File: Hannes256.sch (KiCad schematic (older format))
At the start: 7 parts, among them J1 TED_SOCKET, J2 RAM_SELECTOR, J3 CONN_CS, U1 MOS_7360_TED

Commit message: Routing in progress
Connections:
- net MUX renamed mux
- net clkout renamed CLKOUT
- net ~RAS renamed ~ras

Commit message: ROuting done
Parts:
- added V0: CC_LOGO, Hannes256:cc_by_nc_sa, symbol void:Void
- V1: renamed from V0; value CC_LOGO -> LOGO; footprint Hannes256:cc_by_nc_sa -> Hannes256:logo
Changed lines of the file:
@@
 Sheet 1 3
 Title "Hannes256: C16/+4 256 kB RAM Expansion"
-Date "2023-02-21"
+Date "2023-02-27"
 Rev "3git"
 Comp "SukkoPera"
@@
 $EndComp
 $Comp
-L void:Void V0
+L void:Void V1
 U 1 1 63C4EC1B
 P 15540 9765
-F 0 "V0" H 15618 9811 50  0000 L CNN
-F 1 "CC_LOGO" H 15618 9720 50  0000 L CNN
-F 2 "Hannes256:cc_by_nc_sa" H 15540 9765 50  0001 C CNN
+F 0 "V1" H 15618 9811 50  0000 L CNN
+F 1 "LOGO" H 15618 9720 50  0000 L CNN
+F 2 "Hannes256:logo" H 15540 9765 50  0001 C CNN
 F 3 "" H 15540 9765 50  0001 C CNN
 	1    15540 9765
@@
 Wire Bus Line
 	10425 2375 10425 4285
+$Comp
+L void:Void V0
+U 1 1 64911216
+P 15540 9560
+F 0 "V0" H 15618 9606 50  0000 L CNN
+F 1 "CC_LOGO" H 15618 9515 50  0000 L CNN
+F 2 "Hannes256:cc_by_nc_sa" H 15540 9560 50  0001 C CNN
+F 3 "" H 15540 9560 50  0001 C CNN
+	1    15540 9560
+	1    0    0    -1
+$EndComp
 $EndSCHEMATC

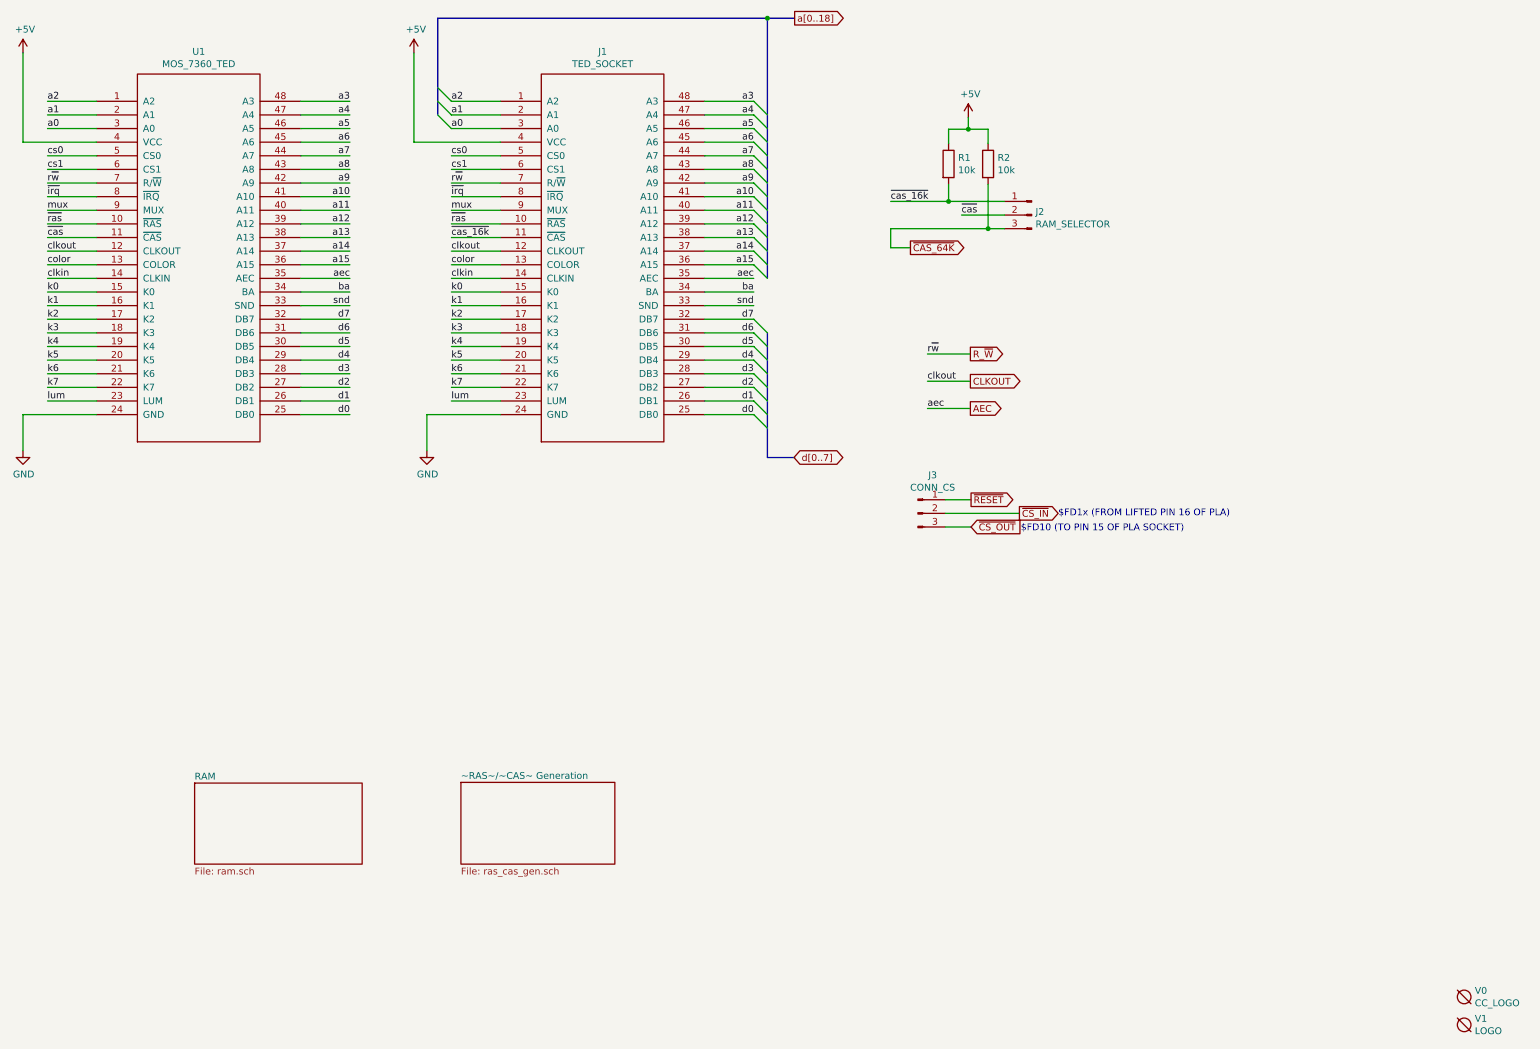
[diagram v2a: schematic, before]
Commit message: Relabel all components
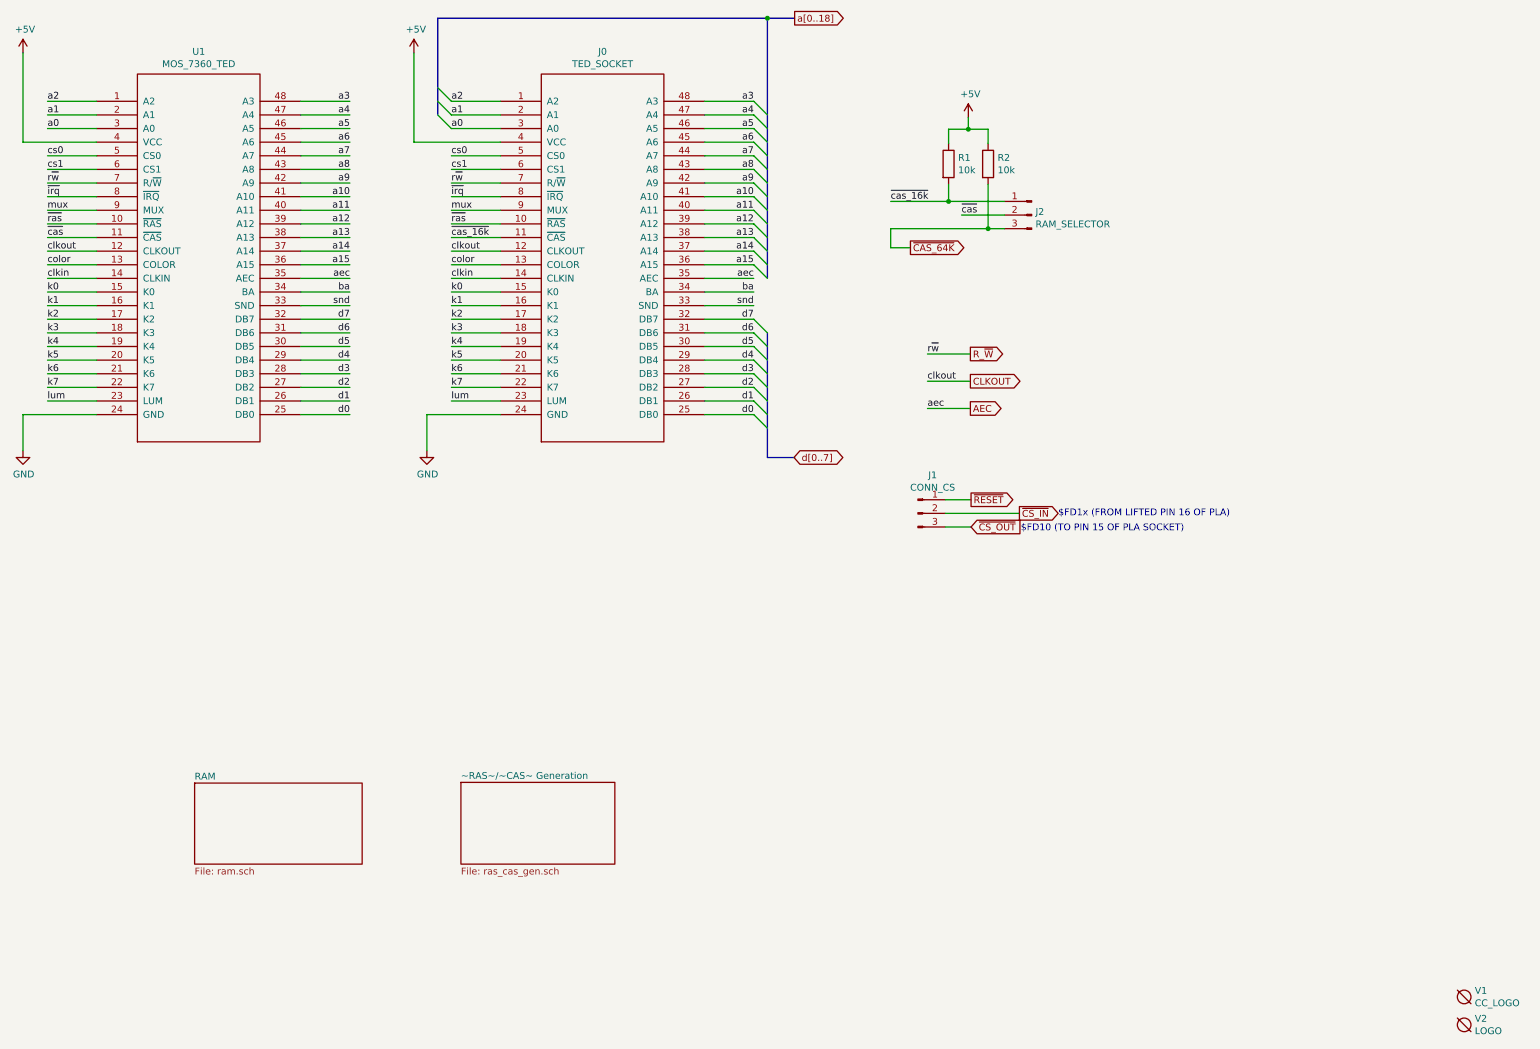
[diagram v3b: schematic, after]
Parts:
- renumbered J1 to J0, J3 to J1, V0 to V1, V1 to V2
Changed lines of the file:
@@
 P 9215 4135
 AR Path="/62E48B71/639188CC" Ref="J?"  Part="1"
-AR Path="/639188CC" Ref="J1"  Part="1"
-F 0 "J1" H 9215 5650 50  0000 C CNN
+AR Path="/639188CC" Ref="J0"  Part="1"
+F 0 "J0" H 9215 5650 50  0000 C CNN
 F 1 "TED_SOCKET" H 9215 5559 50  0000 C CNN
 F 2 "Hannes256:DIP-48_W15.24mm_LongPads_ModSilkS" H 9215 4135 50  0001 C CNN
@@
 P 4960 5550
 AR Path="/62E48B71/639188E6" Ref="#PWR?"  Part="1"
-AR Path="/639188E6" Ref="#PWR04"  Part="1"
-F 0 "#PWR04" H 4960 5300 50  0001 C CNN
+AR Path="/639188E6" Ref="#PWR02"  Part="1"
+F 0 "#PWR02" H 4960 5300 50  0001 C CNN
 F 1 "GND" H 4965 5377 50  0000 C CNN
 F 2 "" H 4960 5550 50  0001 C CNN
@@
 P 7925 5550
 AR Path="/62E48B71/63918986" Ref="#PWR?"  Part="1"
-AR Path="/63918986" Ref="#PWR05"  Part="1"
-F 0 "#PWR05" H 7925 5300 50  0001 C CNN
+AR Path="/63918986" Ref="#PWR04"  Part="1"
+F 0 "#PWR04" H 7925 5300 50  0001 C CNN
 F 1 "GND" H 7930 5377 50  0000 C CNN
 F 2 "" H 7925 5550 50  0001 C CNN
@@
 $FD10 (TO PIN 15 OF PLA SOCKET)
 $Comp
-L Connector:Conn_01x03_Male J3
+L Connector:Conn_01x03_Male J1
 U 1 1 63E0AE52
 P 11530 6010
-F 0 "J3" H 11638 6291 50  0000 C CNN
+F 0 "J1" H 11638 6291 50  0000 C CNN
 F 1 "CONN_CS" H 11638 6200 50  0000 C CNN
 F 2 "Connector_PinHeader_2.54mm:PinHeader_1x03_P2.54mm_Vertical" H 11530 6010 50  0001 C CNN
@@
 ~RESET
 $Comp
-L power:+5V #PWR0103
+L power:+5V #PWR01
 U 1 1 633D4159
 P 4960 2630
-F 0 "#PWR0103" H 4960 2480 50  0001 C CNN
+F 0 "#PWR01" H 4960 2480 50  0001 C CNN
 F 1 "+5V" H 4975 2803 50  0000 C CNN
 F 2 "" H 4960 2630 50  0001 C CNN
@@
 $EndComp
 $Comp
-L power:+5V #PWR0104
+L power:+5V #PWR03
 U 1 1 633D4958
 P 7830 2630
-F 0 "#PWR0104" H 7830 2480 50  0001 C CNN
+F 0 "#PWR03" H 7830 2480 50  0001 C CNN
 F 1 "+5V" H 7845 2803 50  0000 C CNN
 F 2 "" H 7830 2630 50  0001 C CNN
@@
 $EndComp
 $Comp
-L void:Void V1
+L void:Void V2
 U 1 1 63C4EC1B
 P 15540 9765
-F 0 "V1" H 15618 9811 50  0000 L CNN
+F 0 "V2" H 15618 9811 50  0000 L CNN
 F 1 "LOGO" H 15618 9720 50  0000 L CNN
 F 2 "Hannes256:logo" H 15540 9765 50  0001 C CNN
@@
 	11755 3190 11900 3190
 $Comp
-L power:+5V #PWR0105
+L power:+5V #PWR05
 U 1 1 633D56E2
 P 11900 3105
-F 0 "#PWR0105" H 11900 2955 50  0001 C CNN
+F 0 "#PWR05" H 11900 2955 50  0001 C CNN
 F 1 "+5V" H 11915 3278 50  0000 C CNN
 F 2 "" H 11900 3105 50  0001 C CNN
@@
 Text GLabel 11475 4060 2    50   Output ~ 0
 ~CAS_64K
+$Comp
+L void:Void V1
+U 1 1 64911216
+P 15540 9560
+F 0 "V1" H 15618 9606 50  0000 L CNN
+F 1 "CC_LOGO" H 15618 9515 50  0000 L CNN
+F 2 "Hannes256:cc_by_nc_sa" H 15540 9560 50  0001 C CNN
+F 3 "" H 15540 9560 50  0001 C CNN
+	1    15540 9560
+	1    0    0    -1
+$EndComp
 Wire Bus Line
 	8005 2375 8005 3085
@@
 Wire Bus Line
 	10425 2375 10425 4285
-$Comp
-L void:Void V0
-U 1 1 64911216
-P 15540 9560
-F 0 "V0" H 15618 9606 50  0000 L CNN
-F 1 "CC_LOGO" H 15618 9515 50  0000 L CNN
-F 2 "Hannes256:cc_by_nc_sa" H 15540 9560 50  0001 C CNN
-F 3 "" H 15540 9560 50  0001 C CNN
-	1    15540 9560
-	1    0    0    -1
-$EndComp
 $EndSCHEMATC
